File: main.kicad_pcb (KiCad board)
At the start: 2 copper layers, 32 x 32 mm, 51 parts, among them J1 USB_MICRO, J2 Conn_01x02, J3 Conn_01x02, J6 Conn_01x02, J7 AVR-ISP-6, Q1 DMP1045U, Q2 NTLJF3117P, Q3 MMBT3904, SW1 SW_Push, SW2 SW_SPDT, U1 MCP73831, U2 LTC2955-1(DFN), U3 LTC3536, U4 ATtiny13-20SSU

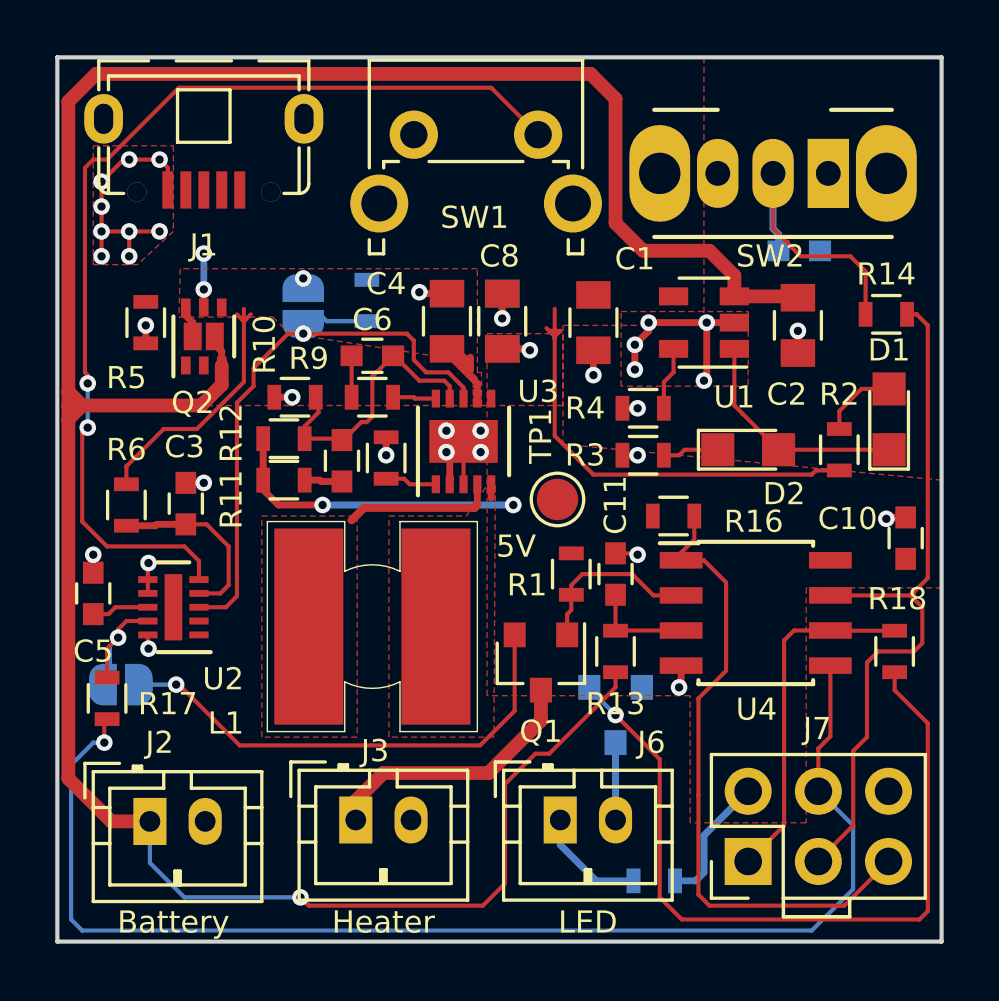
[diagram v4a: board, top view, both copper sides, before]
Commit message: Added power on state LED Updated to KiCAD 5.0
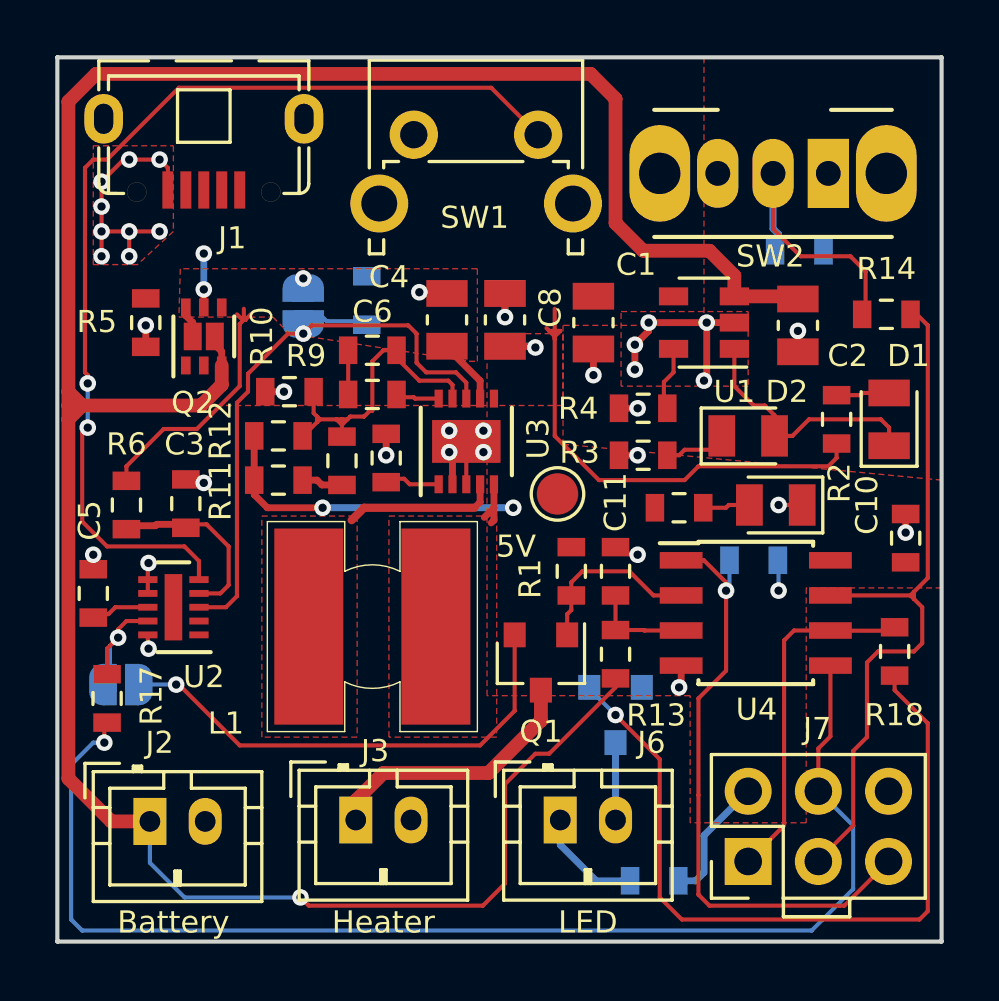
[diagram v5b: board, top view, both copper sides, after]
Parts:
- added D3: LED, LED_SMD:LED_0805_2012Metric, F.Cu at (116.0, 86.2)
- added R19: 1k, Resistor_SMD:R_0603_1608Metric, F.Cu at (112.5, 86.3)
- C1, C2, C4, C8, C9: footprint Capacitors_SMD:C_0805 -> Capacitor_SMD:C_0805_2012Metric
- C10, C11, C12, C3, C5, C6, C7: footprint Capacitors_SMD:C_0603 -> Capacitor_SMD:C_0603_1608Metric
- D1, D2: footprint LEDs:LED_0805 -> LED_SMD:LED_0805_2012Metric
- Q1, Q3: footprint TO_SOT_Packages_SMD:SOT-23 -> Package_TO_SOT_SMD:SOT-23
- R1, R10, R11, R12, R13, R14, R15, R17, R18, R2, R3, R4, R5, R6, R7, R8, R9: footprint Resistors_SMD:R_0603 -> Resistor_SMD:R_0603_1608Metric
- R16: footprint Resistors_SMD:R_0603 -> Resistor_SMD:R_0603_1608Metric; moved to B.Cu
- SW2: footprint Buttons_Switches_THT:SW_CuK_OS102011MA1QN1_SPDT_Angled -> Button_Switch_THT:SW_CuK_OS102011MA1QN1_SPDT_Angled
- U1: footprint TO_SOT_Packages_SMD:SOT-23-5 -> Package_TO_SOT_SMD:SOT-23-5
- U2: footprint Housings_DFN_QFN:DFN-10-1EP_2x3mm_Pitch0.5mm -> Package_DFN_QFN:DFN-10-1EP_2x3mm_P0.5mm_EP0.64x2.4mm
- U3: footprint Housings_DFN_QFN:DFN-10-1EP_3x3mm_Pitch0.5mm -> Package_DFN_QFN:DFN-10-1EP_3x3mm_P0.5mm_EP1.55x2.48mm
- moved R16 3.31 mm to (115.2, 88.2), turned to 180 degrees
- moved R2 1.10 mm to (118.2, 83.1)
- moved D2 0.50 mm to (115.0, 83.7)
- moved R10 0.28 mm to (98.4, 82.1)
- moved R12 0.22 mm to (98.0, 83.7)
- moved C6 0.20 mm to (101.4, 80.6)
- moved R11 0.20 mm to (98.0, 85.3)
- moved TP1 0.20 mm to (108.1, 85.8)
- moved C8 0.11 mm to (106.2, 79.5)
- moved C9 0.11 mm to (106.2, 79.5)
- moved C11 0.10 mm to (110.2, 88.6)
- moved R1 0.10 mm to (108.6, 88.6)
- moved R13 0.10 mm to (110.2, 91.6)
- moved R9 0.10 mm to (101.4, 82.2)
- moved U3 0.10 mm to (104.8, 83.9)
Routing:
- net /Power Supply/DC/DC boost converter/Vsup: track 17.6 -> 13.8 mm
- net /Power Supply/V+5: track 35.7 -> 37.6 mm, vias 4 -> 5
- net Net-(D3-Pad2): track 0.00 -> 1.71 mm
- net Net-(C6-Pad2): track 10.00 -> 11.5 mm
- net Net-(L1-Pad2): track 0.50 -> 1.94 mm
- net Net-(D1-Pad2): track 2.78 -> 1.93 mm
- net Net-(D1-Pad1): track 8.31 -> 9.16 mm
- net GND: track 32.7 -> 33.5 mm, vias 34 -> 35
- net /Power Supply/VUSB: track 18.7 -> 19.5 mm
- net Net-(JP1-Pad2): track 22.9 -> 23.6 mm
- net /Microcontroller/RST: track 23.2 -> 22.5 mm, vias 0 -> 1
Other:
- board text added: "Programmable Heater v1.2 Design: Patrick Baus Date: 2018-06 https://github.com/PatrickBaus"
- board text removed: "Programmable Heater v1.2 Design: Patrick Baus Date: 2018-03 https://github.com/PatrickBaus"
